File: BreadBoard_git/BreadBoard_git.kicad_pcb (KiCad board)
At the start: 2 copper layers, 3 parts, among them J1 24V DC wall plug-iN, U4 SHT45

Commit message: brruuuuuhhhhhh
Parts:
- added C13: C0402C300J5GACTU, ccomp2_5:CAPC10555_55N_KEM, F.Cu at (65.5, 63.5)

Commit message: small updates
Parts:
- added U1: ESP32-S3, ESP32-S3:IC_ESP32-S3, F.Cu at (104.1, 36.9)

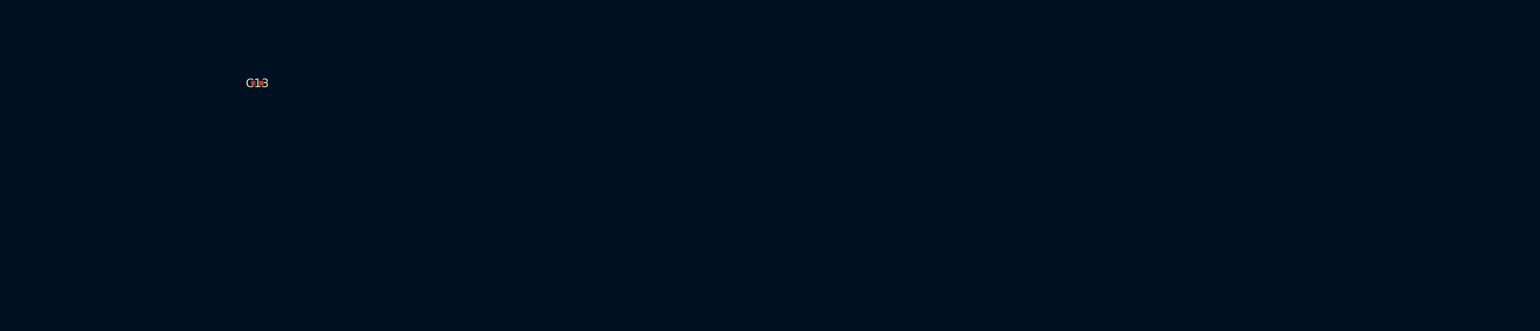
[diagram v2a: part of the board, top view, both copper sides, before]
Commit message: 5V needs to be added
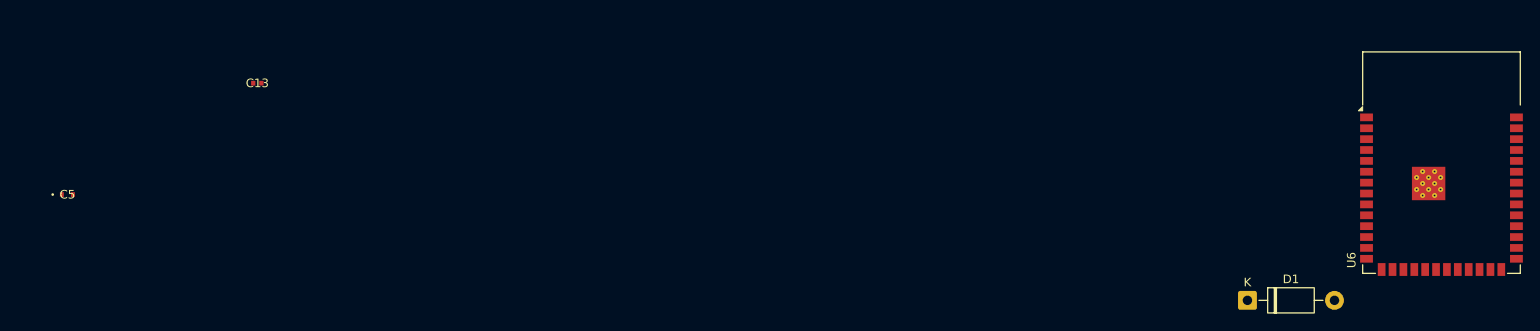
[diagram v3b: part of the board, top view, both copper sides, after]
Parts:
- added C5: C1005X7R1H473K050BB, cinx:CAP_1005_TDK, F.Cu at (43.4, 76.5)
- added D1: 1N5819, Diode_THT:D_DO-41_SOD81_P10.16mm_Horizontal, F.Cu at (181.1, 88.8)
- added U6: ESP32-S3-WROOM-1, RF_Module:ESP32-S3-WROOM-1, F.Cu at (203.8, 72.8)

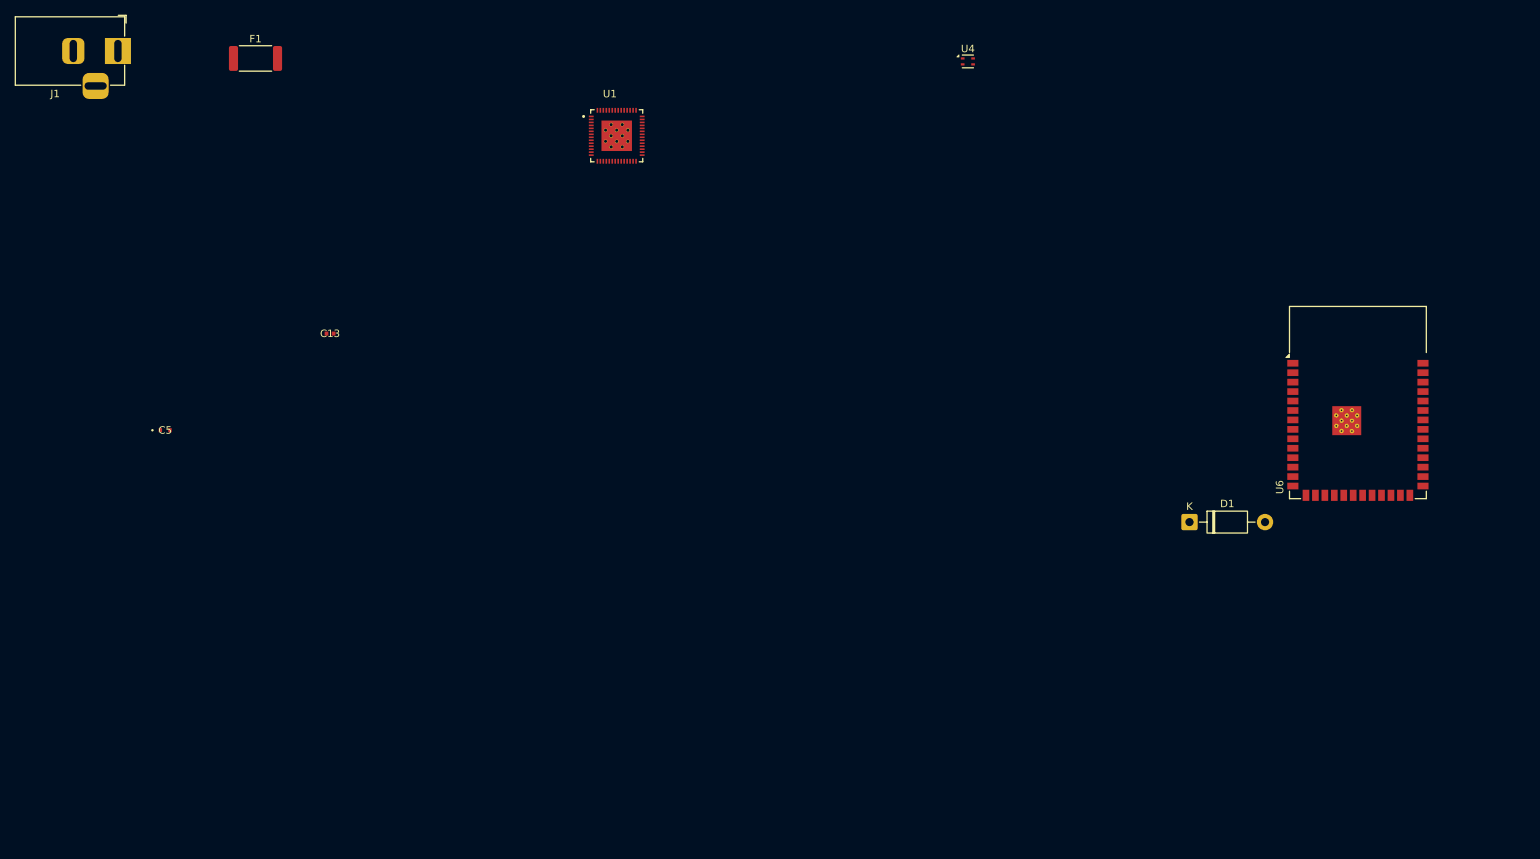
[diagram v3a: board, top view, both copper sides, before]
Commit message: most footprints in
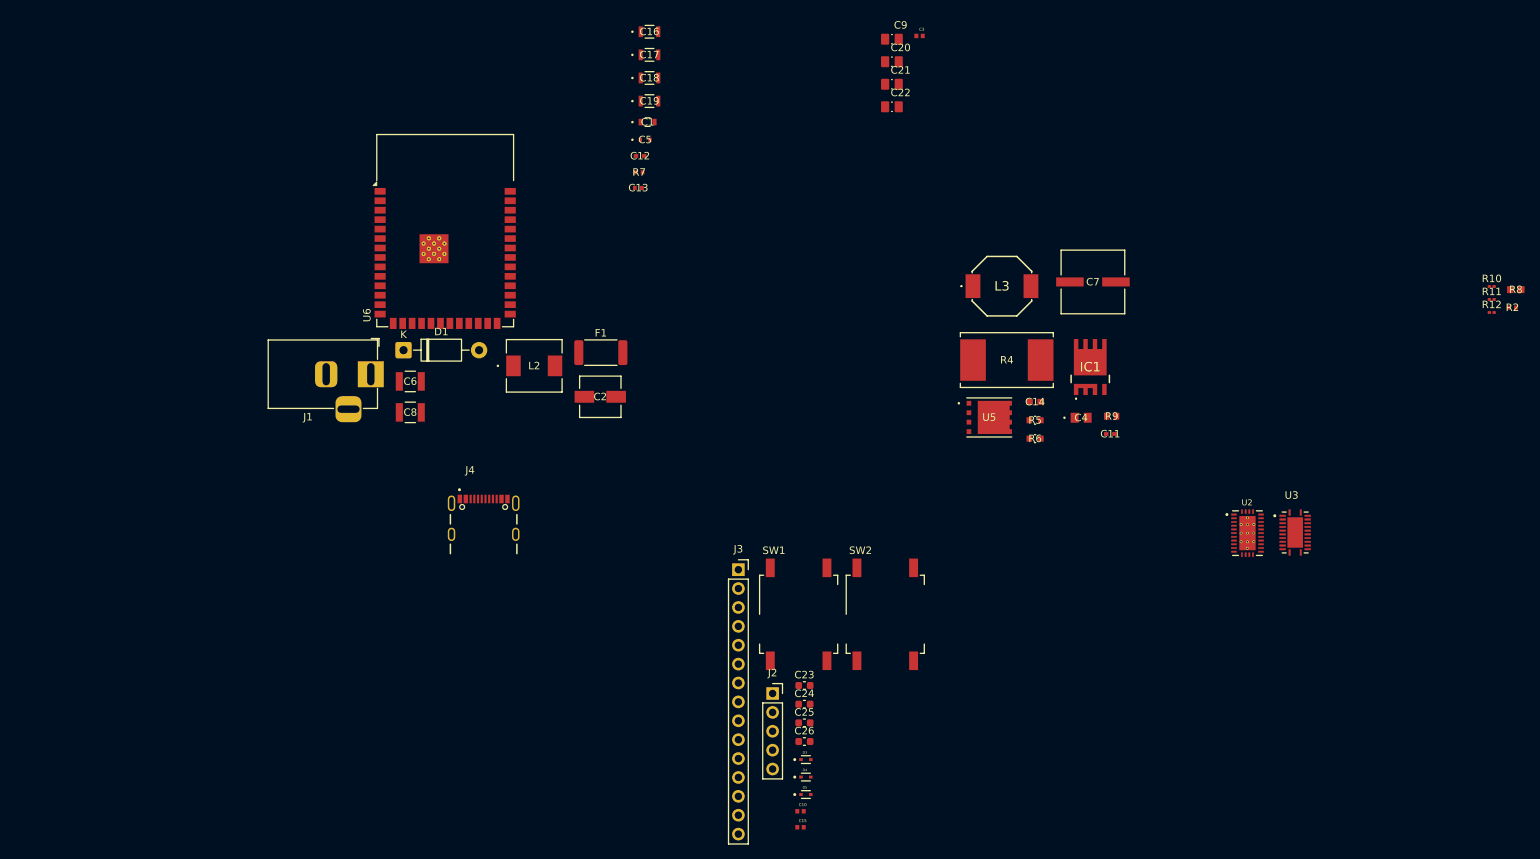
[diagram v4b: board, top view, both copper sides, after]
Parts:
- removed U1: ESP32-S3, ESP32-S3:IC_ESP32-S3
- removed U4: SHT45, Sensor_Humidity:Sensirion_DFN-4_1.5x1.5mm_P0.8mm_SHT4x_NoCentralPad
- added C1: C1608X6S1H474K080AB, coutx:CAP_1608_TDK, F.Cu at (108.2, 35.1)
- added C10: GRM155R71A104KA01D, cvdda_5:CAPC1005X55N, F.Cu at (128.8, 127.7)
- added C11: GRM155R60J474KE19D, cboot:G-155_MUR, F.Cu at (170.5, 77.0)
- added C12: CL05C821JB5NNNC, ccomp_5:CAP_CL05_SAM, F.Cu at (107.2, 39.6)
- added C14: GRM188R71A225KE15D, cvcc_5:G-188_MUR, F.Cu at (160.3, 72.7)
- added C15: GRM155R71A104KA01D, cvdda_5:CAPC1005X55N, F.Cu at (128.8, 129.9)
- added C16: C2012X6S1H155K125AB, cin_5:CAP_2012_TDK, F.Cu at (108.5, 22.9)
- added C17: C2012X6S1H155K125AB, cin_5:CAP_2012_TDK, F.Cu at (108.5, 26.0)
- added C18: C2012X6S1H155K125AB, cin_5:CAP_2012_TDK, F.Cu at (108.5, 29.1)
- added C19: C2012X6S1H155K125AB, cin_5:CAP_2012_TDK, F.Cu at (108.5, 32.2)
- added C2: APXE6R3ARA101ME61G, cout:CHEMI-E61, F.Cu at (101.9, 72.0)
- added C20: MSAST21GBB5106MTNA01, cout_5:CAPC2012X145N, F.Cu at (141.1, 26.9)
- added C21: MSAST21GBB5106MTNA01, cout_5:CAPC2012X145N, F.Cu at (141.1, 30.0)
- added C22: MSAST21GBB5106MTNA01, cout_5:CAPC2012X145N, F.Cu at (141.1, 33.0)
- added C23: 1uF, Capacitor_SMD:C_0603_1608Metric, F.Cu at (129.3, 110.8)
- added C24: 100nF, Capacitor_SMD:C_0603_1608Metric, F.Cu at (129.3, 113.3)
- added C25: 10uF, Capacitor_SMD:C_0603_1608Metric, F.Cu at (129.3, 115.8)
- added C26: 10uF, Capacitor_SMD:C_0603_1608Metric, F.Cu at (129.3, 118.4)
- added C3: GRM1555C1H160JA01D, cff:CAPC1005X55N, F.Cu at (144.8, 23.5)
- added C4: GRM21BR71A225KA01L, cvcc:CAP_GRM21_MUR, F.Cu at (166.5, 74.8)
- added C6: CL32A106KBJNNNE, cin:CAP_CL32_SAM, F.Cu at (76.3, 69.9)
- added C7: UUD1V101MNL1GS, cbulk:U2-P_NCH, F.Cu at (168.1, 56.6)
- added C8: CL32A106KBJNNNE, cin:CAP_CL32_SAM, F.Cu at (76.3, 74.1)
- added C9: MSAST21GBB5106MTNA01, cout_5:CAPC2012X145N, F.Cu at (141.1, 23.9)
- added D3: LESD5D5.0CT1G, led:TVS_LESD5D5.0CT1G, F.Cu at (129.5, 120.8)
- added D4: LESD5D5.0CT1G, led:TVS_LESD5D5.0CT1G, F.Cu at (129.5, 123.1)
- added D5: LESD5D5.0CT1G, led:TVS_LESD5D5.0CT1G, F.Cu at (129.5, 125.5)
- added IC1: IAUCN04S7L028ATMA1, M1_5:IAUC120N06S5N011ATMA1, F.Cu at (167.8, 68.1)
- added J2: Conn_01x05_Socket, Connector_PinSocket_2.54mm:PinSocket_1x05_P2.54mm_Vertical, F.Cu at (125.0, 111.9)
- added J3: Conn_01x15_Socket, Connector_PinSocket_2.54mm:PinSocket_1x15_P2.54mm_Vertical, F.Cu at (120.4, 95.2)
- added J4: USB4105-GF-A, usb:GCT_USB4105-GF-A, F.Cu at (86.2, 90.5)
- added L2: CDEP63MENP-R68MC, L1_5:IND_CDEP63MENP-R68MC_SUM, F.Cu at (93.0, 67.8)
- added L3: SRU8043-3R9Y, L1:SRU80433R9Y, F.Cu at (155.9, 57.1)
- added R10: 10k, Resistor_SMD:R_0201_0603Metric, F.Cu at (221.8, 57.2)
- added R11: 5.1K, Resistor_SMD:R_0201_0603Metric, F.Cu at (221.8, 58.9)
- added R12: 5.1K, Resistor_SMD:R_0201_0603Metric, F.Cu at (221.8, 60.7)
- added R2: CRCW0402100KFKED, rcomp_5:RES_CRCW_0402, F.Cu at (224.5, 60.0)
- added R4: WSR23L000FEA, rsense_5:WSR, F.Cu at (156.5, 67.1)
- added R5: RC0603FR-079K53L, rconfig_5:RC0603N_YAG, F.Cu at (160.3, 75.2)
- added R6: RC0603FR-0740K2L, rconfig_5:RC0603N_YAG, F.Cu at (160.3, 77.6)
- added R7: CRCW04024K87FKED, rcomp_5:RES_CRCW_0402, F.Cu at (107.1, 41.8)
- added R8: CRCW0603100KFKEA, rpg_5:RES_CRCW_0603_VIS, F.Cu at (225.0, 57.6)
- added R9: CRCW060347K5FKEA, rvdda_5:RES_CRCW_0603, F.Cu at (170.6, 74.6)
- added SW1: SW_DPST_x2, Button_Switch_SMD:SW_MEC_5GSH9, F.Cu at (128.5, 101.2)
- added SW2: SW_DPST_x2, Button_Switch_SMD:SW_MEC_5GSH9, F.Cu at (140.2, 101.2)
- added U2: LM73605RNPR, LM7:QFN50P600X400X80-31N, F.Cu at (188.9, 90.3)
- added U3: LM5148RGYR, LM5:QFN50P550X350X100-25N, F.Cu at (195.3, 90.2)
- added U5: CSD17577Q5A, M2_5:DQJ8, F.Cu at (154.2, 74.8)
- moved U6 124.9 mm to (81.0, 49.6)
- moved D1 108.2 mm to (75.4, 65.7)
- moved C5 75.4 mm to (107.9, 37.4)
- moved F1 61.0 mm to (101.9, 66.1)
- moved J1 55.2 mm to (71.0, 69.0)
- moved C13 45.9 mm to (107.0, 43.9)
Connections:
- C5 pad 2: Net-(U2-EN) -> VBUS

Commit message: updates
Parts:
- removed C15: GRM155R71A104KA01D, cvdda_5:CAPC1005X55N
- removed C26: 10uF, Capacitor_SMD:C_0603_1608Metric
- removed D3, D4, D5: LESD5D5.0CT1G, led:TVS_LESD5D5.0CT1G
- removed IC1: IAUCN04S7L028ATMA1, M1_5:IAUC120N06S5N011ATMA1
- removed J3: Conn_01x15_Socket, Connector_PinSocket_2.54mm:PinSocket_1x15_P2.54mm_Vertical
- removed J4: USB4105-GF-A, usb:GCT_USB4105-GF-A
- removed L3: SRU8043-3R9Y, L1:SRU80433R9Y
- removed R10: 10k, Resistor_SMD:R_0201_0603Metric
- removed R12: 5.1K, Resistor_SMD:R_0201_0603Metric
- removed R9: CRCW060347K5FKEA, rvdda_5:RES_CRCW_0603
- added C33: C, Capacitor_SMD:C_0201_0603Metric_Pad0.64x0.40mm_HandSolder, F.Cu at (231.1, 149.0)
- added C35: GRM32ER71H475KA88L, footprints:CAPC3225X270N, F.Cu at (62.8, 178.9)
- added D2: D_Schottky, Diode_SMD:D_SOD-523, F.Cu at (42.0, 83.5)
- added JP1: Jumper_3_Open, Connector_Samtec_HPM_THT:Samtec_HPM-03-01-x-S_Straight_1x03_Pitch5.08mm, F.Cu at (106.5, 58.8)
- added L1: WE-XHMI_5050, footprints:WE-XHMI_5050, F.Cu at (31.2, 166.9)
- added Q1: BC818, Package_TO_SOT_SMD:SOT-23, F.Cu at (129.6, 171.0)
- added Q2: BC818, Package_TO_SOT_SMD:SOT-23, F.Cu at (129.6, 175.4)
- added Q3: CSD18512Q5B, footprints:TRANS_CSD18512Q5B, F.Cu at (249.3, 69.3)
- added Q4: CSD18512Q5B, footprints:TRANS_CSD18512Q5B, F.Cu at (249.3, 75.9)
- added Q5: RQ3E110AJTB, footprints:HSMT8_ROM-L, F.Cu at (134.5, 83.7)
- added Q6: RQ3E110AJTB, footprints:HSMT8_ROM-L, F.Cu at (134.5, 88.4)
- added R1: 1M, Resistor_SMD:R_0201_0603Metric_Pad0.64x0.40mm_HandSolder, F.Cu at (67.1, 89.5)
- added R14: CRCW0402100KFKED, footprints:RES_CRCW_0402_VIS-L, F.Cu at (40.4, 153.3)
- added R15: RC0603FR-0724K9L, footprints:RC0603N_YAG-L, F.Cu at (28.3, 160.3)
- added R16: RC0603FR-079K53L, footprints:RC0603N_YAG-L, F.Cu at (256.5, 45.8)
- added R17: CRCW04021K00FKED, footprints:RESC1005X40N, F.Cu at (47.4, 180.0)
- added R18: 150, Resistor_SMD:R_0603_1608Metric_Pad0.98x0.95mm_HandSolder, F.Cu at (84.6, 159.0)
- added R19: WSR23L000FEA, footprints:WSR-L, F.Cu at (237.6, 70.3)
- added R3: CRCW060347K5FKEA, footprints:RES_CRCW_0603-L, F.Cu at (224.0, 84.5)
- added U1: TPD4E02B04DQA, Package_SON:USON-10_2.5x1.0mm_P0.5mm, F.Cu at (58.6, 78.5)
- added U4: AMS1117-3.3, Package_TO_SOT_SMD:SOT-223-3_TabPin2, F.Cu at (101.0, 156.1)
- C1: value C1608X6S1H474K080AB -> C2012X6S1H155K125AB; footprint coutx:CAP_1608_TDK -> footprints:CAP_2012_TDK-L
- C10: value GRM155R71A104KA01D -> CL05C821JB5NNNC; footprint cvdda_5:CAPC1005X55N -> footprints:CAP_CL05_SAM-L
- C11: value GRM155R60J474KE19D -> C0402C300J5GACTU; footprint cboot:G-155_MUR -> footprints:CAPC10555_55N_KEM-L
- C12: value CL05C821JB5NNNC -> MSAST21GBB5106MTNA01; footprint ccomp_5:CAP_CL05_SAM -> footprints:CAPC2012X145N
- C13: value C0402C300J5GACTU -> GRM32ER71H475KA88L; footprint ccomp2_5:CAPC10555_55N_KEM -> footprints:CAPC3225X270N
- C14: value GRM188R71A225KE15D -> GRM155R71A104KA01D; footprint cvcc_5:G-188_MUR -> footprints:CAPC1005X55N
- C16: value C2012X6S1H155K125AB -> GRM155R61A106ME11D; footprint cin_5:CAP_2012_TDK -> footprints:RC0603N_YAG-L
- C17: value C2012X6S1H155K125AB -> GRM155R71A104KA01D; footprint cin_5:CAP_2012_TDK -> footprints:G-155_MUR-L
- C18: value C2012X6S1H155K125AB -> C0201X5R104K100NTA; footprint cin_5:CAP_2012_TDK -> footprints:RC0603N_YAG-L
- C19: value C2012X6S1H155K125AB -> CC0805JRNPO9BN120; footprint cin_5:CAP_2012_TDK -> footprints:CAP_CC0805_YAG-L
- C2: value APXE6R3ARA101ME61G -> GRM188R60J105KA01D; footprint cout:CHEMI-E61 -> footprints:G-188_MUR-L
- C20: value MSAST21GBB5106MTNA01 -> GRM31CR61A107MEA8K; footprint cout_5:CAPC2012X145N -> footprints:CAPC3216X190N
- C21: value MSAST21GBB5106MTNA01 -> C0201X5R104K100NTA; footprint cout_5:CAPC2012X145N -> footprints:RC0603N_YAG-L
- C22: value MSAST21GBB5106MTNA01 -> GRM188R61A226ME15D; footprint cout_5:CAPC2012X145N -> footprints:RC0603N_YAG-L
- C23: value 1uF -> MSAST21GBB5106MTNA01; footprint Capacitor_SMD:C_0603_1608Metric -> footprints:CAPC2012X145N
- C24: value 100nF -> MSAST21GBB5106MTNA01; footprint Capacitor_SMD:C_0603_1608Metric -> footprints:CAPC2012X145N
- C25: value 10uF -> MSAST21GBB5106MTNA01; footprint Capacitor_SMD:C_0603_1608Metric -> footprints:CAPC2012X145N
- C3: value GRM1555C1H160JA01D -> C2012X6S1H155K125AB; footprint cff:CAPC1005X55N -> footprints:CAP_2012_TDK-L
- C4: value GRM21BR71A225KA01L -> C2012X6S1H155K125AB; footprint cvcc:CAP_GRM21_MUR -> footprints:CAP_2012_TDK-L
- C5: value C1005X7R1H473K050BB -> C1005X5R1V474K050BC; footprint cinx:CAP_1005_TDK -> footprints:CAPC1005X55N
- C6: value CL32A106KBJNNNE -> C2012X6S1H155K125AB; footprint cin:CAP_CL32_SAM -> footprints:CAP_2012_TDK-L
- C7: value UUD1V101MNL1GS -> GRM155R71A104KA01D; footprint cbulk:U2-P_NCH -> footprints:G-155_MUR-L
- C8: value CL32A106KBJNNNE -> C1005X5R1V474K050BC; footprint cin:CAP_CL32_SAM -> footprints:CAPC1005X55N
- C9: value MSAST21GBB5106MTNA01 -> GRM188R71A225KE15D; footprint cout_5:CAPC2012X145N -> footprints:G-188_MUR-L
- D1: value 1N5819 -> SMBJ28A; footprint Diode_THT:D_DO-41_SOD81_P10.16mm_Horizontal -> footprints:DIOM5436X244N
- F1: value 0.1 Omh -> TR/3216TD12-R; footprint Resistor_SMD:R_2512_6332Metric -> footprints:FUS_CB_3216TD
- J1: value 24V DC wall plug-iN -> PD-40; footprint Connector_BarrelJack:BarrelJack_Horizontal -> footprints:CUI_PD-40
- J2: value Conn_01x05_Socket -> USB_C_Receptacle_USB2.0_14P; footprint Connector_PinSocket_2.54mm:PinSocket_1x05_P2.54mm_Vertical -> Connector_USB:USB_C_Receptacle_HRO_TYPE-C-31-M-12
- L2: footprint L1_5:IND_CDEP63MENP-R68MC_SUM -> footprints:IND_CDEP63MENP-R68MC_SUM-L
- R11: value 5.1K -> RC0603FR-0740K2L; footprint Resistor_SMD:R_0201_0603Metric -> footprints:RC0603N_YAG-L
- R2: value CRCW0402100KFKED -> GRM188R60J105KA01D; footprint rcomp_5:RES_CRCW_0402 -> footprints:RESC2012X50N
- R4: value WSR23L000FEA -> 5k1; footprint rsense_5:WSR -> Resistor_SMD:R_0201_0603Metric_Pad0.64x0.40mm_HandSolder
- R5: value RC0603FR-079K53L -> CRCW0603100KFKEA; footprint rconfig_5:RC0603N_YAG -> footprints:RES_CRCW_0603_VIS-L
- R6: value RC0603FR-0740K2L -> 5k1; footprint rconfig_5:RC0603N_YAG -> Resistor_SMD:R_0201_0603Metric_Pad0.64x0.40mm_HandSolder
- R7: footprint rcomp_5:RES_CRCW_0402 -> footprints:RES_CRCW_0402-L
- R8: value CRCW0603100KFKEA -> CRCW0402100KFKED; footprint rpg_5:RES_CRCW_0603_VIS -> footprints:RES_CRCW_0402_VIS-L
- SW1, SW2: value SW_DPST_x2 -> SKRPADE010; footprint Button_Switch_SMD:SW_MEC_5GSH9 -> footprints:SKRPADE010_AAL
- U2: value LM73605RNPR -> LM61460AANRJRR; footprint LM7:QFN50P600X400X80-31N -> footprints:IC_LM61460AANRJRR
- U3: footprint LM5:QFN50P550X350X100-25N -> footprints:QFN50P550X350X100-25N
- U5: value CSD17577Q5A -> ESP32-S3-WROOM-1; footprint M2_5:DQJ8 -> RF_Module:ESP32-S3-WROOM-1
- U6: value ESP32-S3-WROOM-1 -> CP2102N-A02-GQFN28R; footprint RF_Module:ESP32-S3-WROOM-1 -> footprints:IC_CP2102N-A02-GQFN28R
- moved R2 232.4 mm to (24.4, 178.2)
- moved R8 207.0 mm to (40.4, 151.4)
- moved C6 191.1 mm to (265.3, 42.0)
- moved C20 189.1 mm to (30.2, 180.1)
- moved L2 172.1 mm to (260.4, 27.9)
- moved U2 168.5 mm to (38.5, 166.1)
- moved U6 164.0 mm to (221.4, 134.4)
- moved R7 161.8 mm to (268.6, 32.9)
- moved C1 157.1 mm to (265.3, 33.4)
- moved C14 154.3 mm to (47.4, 177.8)
- moved C10 153.4 mm to (268.4, 64.2)
- moved C12 153.2 mm to (260.3, 33.5)
- moved C23 150.6 mm to (260.3, 36.5)
- moved C24 150.4 mm to (260.3, 39.6)
- moved C25 150.1 mm to (260.3, 42.6)
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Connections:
- C1 pad 2: 3.3V -> +VBUS
- C10 pad 1: Net-(U3-SW) -> Net-(C10-Pad1)
- C10 pad 2: Net-(U3-CBOOT) -> Net-(C10-Pad2)
- C11 pad 1: Net-(U2-CBOOT) -> Net-(C10-Pad1)
- C11 pad 2: Net-(U2-SW_1) -> Net-(U3-EXTCOMP)
- C12 pad 1: Net-(C12-Pad1) -> GND
- C12 pad 2: Net-(C12-Pad2) -> Heater Vcc 1
- C13 pad 1: Net-(C12-Pad1) -> GND
- C13 pad 2: Net-(U3-EXTCOMP) -> +VBUS
- C14 pad 1: GND -> Net-(U2-CBOOT)
- C14 pad 2: Net-(U3-VCC) -> Net-(U2-SW)
- C16 pad 1: GND -> +5V_Jump
- C16 pad 2: Net-(U3-EN) -> GND
- C17 pad 1: GND -> Net-(U3-SW)
- C17 pad 2: Net-(U3-EN) -> Net-(U3-CBOOT)
- C18 pad 1: GND -> +5V_Jump
- C18 pad 2: Net-(U3-EN) -> GND
- C19 pad 1: GND -> +5V_input
- C19 pad 2: Net-(U3-EN) -> Net-(C19-Pad2)
- C2 pad 1: GND -> Net-(U2-VCC)
- C2 pad 2: 3.3V -> GND
- C20 pad 1: Heater Vcc -> +5V_input
- C20 pad 2: Heater Vcc -> GND
- C21 pad 1: Heater Vcc -> +3.3V
- C21 pad 2: Heater Vcc -> GND
- C22 pad 1: Heater Vcc -> +3.3V
- C22 pad 2: Heater Vcc -> GND
- C23 pad 1: Net-(SW1A-B) -> GND
- C23 pad 2: GND -> Heater Vcc 1
- C24 pad 1: +3.3V -> GND
- C24 pad 2: GND -> Heater Vcc 1
- C25 pad 1: +3.3V -> GND
- C25 pad 2: GND -> Heater Vcc 1
- C3 pad 1: Net-(U2-FB) -> GND
- C3 pad 2: 3.3V -> +VBUS
- C4 pad 2: Net-(U2-VCC) -> +VBUS
- C5 pad 1: GND -> +VBUS
- C5 pad 2: VBUS -> GND
- C6 pad 2: VBUS -> +VBUS
- C7 pad 1: VBUS -> GND
- C7 pad 2: GND -> Net-(U3-PFM/SYNC)
- C8 pad 1: GND -> +VBUS
- C8 pad 2: VBUS -> GND
- C9 pad 1: Heater Vcc -> GND
- C9 pad 2: Heater Vcc -> Net-(U3-VCC)
- F1 pad 1: Net-(J1-Pin_1) -> Net-(F1-Pad1)
- F1 pad 2: Net-(D2-PadA) -> +VBUS
- J1 pad 1: Net-(J1-Pin_1) -> Net-(F1-Pad1)
- J1 pad 2: GND -> Net-(F1-Pad1)
- J1 pad 3: (no net) -> GND
- R11 pad 1: Net-(J4-CC2) -> Net-(U3-CNFG)
- R2 pad 1: Net-(U2-FB) -> GND
- R2 pad 2: 3.3V -> Net-(U2-RT)
- R4 pad 1: Net-(U3-ISNS+) -> Net-(J2-CC2)
- R4 pad 2: Heater Vcc -> GND
- R5 pad 1: Net-(U3-RT) -> Net-(U3-VCC)
- R5 pad 2: GND -> Net-(U3-PG/SYNCOUT)
- R6 pad 1: Net-(U3-CNFG) -> Net-(J2-CC1)
- R7 pad 2: Net-(C12-Pad2) -> Net-(C10-Pad2)
- R8 pad 1: Net-(U3-PG/SYNCOUT) -> Net-(U2-PGOOD)
- R8 pad 2: Net-(U3-VCC) -> +5V_input
- SW1 pad 1: GND -> CHIP_PU
- SW1 pad 2: Net-(SW1A-B) -> unconnected-(SW1-Pad2)
- SW1 pad 3: (no net) -> GND
- SW1 pad 4: (no net) -> unconnected-(SW1-Pad4)
- SW2 pad 1: GND -> BOOT
- SW2 pad 2: Net-(SW1A-B) -> unconnected-(SW2-Pad2)
- SW2 pad 3: (no net) -> GND
- SW2 pad 4: (no net) -> unconnected-(SW2-Pad4)
- U2 pad 1: Net-(U2-SW_1) -> +5V_input
- U2 pad 10: unconnected-(U2-SS/TRK-Pad10) -> Net-(U2-SW)
- U2 pad 11: Net-(U2-FB) -> GND
- U2 pad 12: unconnected-(U2-NC_12-Pad12) -> +VBUS
- U2 pad 13: unconnected-(U2-NC_13-Pad13) -> Net-(U2-CBOOT)
- U2 pad 14: unconnected-(U2-NC_14-Pad14) -> Net-(U2-CBOOT)
- U2 pad 2: Net-(U2-SW_1) -> Net-(U2-VCC)
- U2 pad 3: Net-(U2-SW_1) -> GND
- U2 pad 4: Net-(U2-SW_1) -> Net-(U2-FB)
- U2 pad 5: Net-(U2-SW_1) -> Net-(U2-PGOOD)
- U2 pad 6: Net-(U2-CBOOT) -> Net-(U2-RT)
- U2 pad 7: Net-(U2-VCC) -> unconnected-(U2-EN/SYNC-Pad7)
- U2 pad 8: GND -> +VBUS
- U2 pad 9: unconnected-(U2-RT-Pad9) -> GND
- U3 pad 12: Net-(U3-EN) -> +VBUS
- U3 pad 19: Net-(U3-EN) -> +VBUS
- U3 pad 21: Heater Vcc -> Heater Vcc 1
- U5 pad 1: unconnected-(U5-S-Pad1) -> GND
- U5 pad 2: unconnected-(U5-S-Pad2) -> +3.3V_esp
- U5 pad 3: unconnected-(U5-S-Pad3) -> CHIP_PU
- U5 pad 6: unconnected-(U5-D-Pad6) -> gpio6
- U5 pad 7: unconnected-(U5-D-Pad7) -> gpio7
- U6 pad 1: GND -> unconnected-(U6-DCD-Pad1)
- U6 pad 11: unconnected-(U6-IO18-Pad11) -> Net-(U6-~{SUSPEND})
- U6 pad 12: Net-(J3-Pin_11) -> unconnected-(U6-SUSPEND-Pad12)
- U6 pad 13: Net-(J4-DN1) -> unconnected-(U6-CHREN-Pad13)
- U6 pad 14: Net-(J4-DP1) -> unconnected-(U6-CHR1-Pad14)
- U6 pad 17: Net-(J3-Pin_9) -> unconnected-(U6-GPIO2_RS485-Pad17)
- U6 pad 18: Net-(J3-Pin_8) -> unconnected-(U6-GPIO1_RXT-Pad18)
- U6 pad 19: Net-(J3-Pin_7) -> unconnected-(U6-GPIO0_TXT-Pad19)
- U6 pad 2: +3.3V -> unconnected-(U6-RI/CLK-Pad2)
- U6 pad 20: Net-(J3-Pin_5) -> unconnected-(U6-GPIO6-Pad20)
- U6 pad 21: Net-(J3-Pin_6) -> unconnected-(U6-GPIO5-Pad21)
- U6 pad 24: unconnected-(U6-IO47-Pad24) -> rts
- U6 pad 25: unconnected-(U6-IO48-Pad25) -> U0RXD
- U6 pad 26: unconnected-(U6-IO45-Pad26) -> U0TXD
- U6 pad 27: Net-(SW1A-B) -> unconnected-(U6-DSR-Pad27)
- U6 pad 28: unconnected-(U6-IO35-Pad28) -> dtr
- U6 pad 29: unconnected-(U6-IO36-Pad29) -> GND
- U6 pad 3: Net-(SW1A-B) -> GND
- U6 pad 5: Net-(Q5-Gate) -> unconnected-(U6-D--Pad5)
- U6 pad 6: Net-(Q4-Gate) -> +3.3V
- U6 pad 7: Net-(Q3-Gate) -> +3.3V
- U6 pad 8: Net-(J2-Pin_5) -> Net-(U6-VBUS)
- U6 pad 9: Net-(J2-Pin_4) -> Net-(U6-~{RST})

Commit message: layout!
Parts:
- removed C33: C, Capacitor_SMD:C_0201_0603Metric_Pad0.64x0.40mm_HandSolder
- removed Q1, Q2: BC818, Package_TO_SOT_SMD:SOT-23
- removed U6: CP2102N-A02-GQFN28R, footprints:IC_CP2102N-A02-GQFN28R
- added C15: GRM033R61A104KE15D, footprints:CAPC0603X33N, F.Cu at (232.2, 76.4)
- added C26: 0402B104K500HI, Capacitor_SMD:C_0402_1005Metric_Pad0.74x0.62mm_HandSolder, F.Cu at (54.4, 170.4)
- added C27: 10uF, footprints:G-155_MUR-L, F.Cu at (216.6, 43.3)
- added C28: 100nF, footprints:CAPC0603X33N, F.Cu at (217.5, 43.4)
- added C32: 1uF/16V, footprints:CAPC0603X33N, F.Cu at (217.2, 44.8)
- added C34: 0402B104K500HI, Capacitor_SMD:C_0402_1005Metric_Pad0.74x0.62mm_HandSolder, F.Cu at (54.4, 172.4)
- added D3: LED, LED_SMD:LED_0201_0603Metric, F.Cu at (203.4, 42.4)
- added J3: Conn_01x02_Pin, Connector_PinHeader_1.00mm:PinHeader_1x02_P1.00mm_Vertical, F.Cu at (238.8, 43.4)
- added R23: 10K, Resistor_SMD:R_0201_0603Metric, F.Cu at (216.1, 44.9)
- added R25: 47, Resistor_SMD:R_0201_0603Metric_Pad0.64x0.40mm_HandSolder, F.Cu at (261.3, 69.6)
- added R26: 47, Resistor_SMD:R_0201_0603Metric_Pad0.64x0.40mm_HandSolder, F.Cu at (261.3, 71.3)
- added R27: 100k, Resistor_SMD:R_0201_0603Metric_Pad0.64x0.40mm_HandSolder, F.Cu at (261.3, 73.1)
- added R28: 100k, Resistor_SMD:R_0201_0603Metric_Pad0.64x0.40mm_HandSolder, F.Cu at (261.3, 74.8)
- added R9: 10k, Resistor_SMD:R_0201_0603Metric, F.Cu at (41.9, 168.5)
- C16: value GRM155R61A106ME11D -> 10uF
- C18, C21: value C0201X5R104K100NTA -> 100nF
- C22: value GRM188R61A226ME15D -> 22uF
- R1: value 1M -> 10k; footprint Resistor_SMD:R_0201_0603Metric_Pad0.64x0.40mm_HandSolder -> Resistor_SMD:R_0201_0603Metric
- moved J2 202.5 mm to (232.7, 82.5)
- moved D2 188.5 mm to (230.4, 76.4), turned to 180 degrees
- moved U1 175.7 mm to (234.3, 76.2), turned to -90 degrees
- moved R4 170.5 mm to (237.0, 76.8)
- moved R6 165.7 mm to (231.9, 75.1)
- moved R18 164.6 mm to (203.3, 45.0), turned to 90 degrees
- moved U4 156.7 mm to (211.2, 44.7)
- moved L2 153.9 mm to (152.9, 138.0)
- moved C1 146.5 mm to (150.1, 123.9)
- moved C3 146.5 mm to (150.1, 126.8)
- moved C4 146.5 mm to (150.1, 129.6)
- moved C6 146.5 mm to (150.1, 132.5)
- moved C22 146.5 mm to (205.6, 43.5), turned to 180 degrees
- moved C21 144.3 mm to (205.5, 44.7), turned to 180 degrees
- moved C18 141.5 mm to (205.6, 47.1), turned to 180 degrees
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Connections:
- J1 pad 2: Net-(F1-Pad1) -> GND
- J1 pad 4: GND -> Net-(F1-Pad1)
- J2 pad S1: Net-(J2-SHIELD) -> GND
- R1 pad 1: Net-(J2-SHIELD) -> +3.3V
- R1 pad 2: GND -> CHIP_PU
- U5 pad 13: unconnected-(U5-USB_D--Pad13) -> Data-
- U5 pad 14: unconnected-(U5-USB_D+-Pad14) -> Data+
- U5 pad 2: +3.3V_esp -> +3.3V
- U5 pad 36: U0RXD -> unconnected-(U5-RXD0-Pad36)
- U5 pad 37: U0TXD -> unconnected-(U5-TXD0-Pad37)
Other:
- board outline added: 105.9 x 45.9 mm
